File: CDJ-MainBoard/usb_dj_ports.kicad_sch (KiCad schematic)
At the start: 33 parts, among them J10 USB_DJ_STICK (USB3_A), J11 USB_SCREEN (USB3_A), J8 AUX POWER USB_A, J9 USB_C_Receptacle_USB2.0_16P, U1 Compute_Module_5_Functional, U3 AP2553W6-7, U4 AP2553W6-7, U5 AP2553W6-7, U6 USBLC6-2SC6, U7 USBLC6-2SC6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

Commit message: Add connectors for sections of inputs, and list of all inputs in XLSX
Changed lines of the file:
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@@
-	)
-	(junction
-		(at 35.56 167.64)
-		(diameter 0)
-		(color 0 0 0 0)
 	)
 	(junction
@@
 		)
 		(stroke
-			(width 0)
-			(type default)
-		)
-	)
-	(wire
-		(pts
-			(xy 35.56 167.64) (xy 30.48 167.64)
-		)
-		(stroke

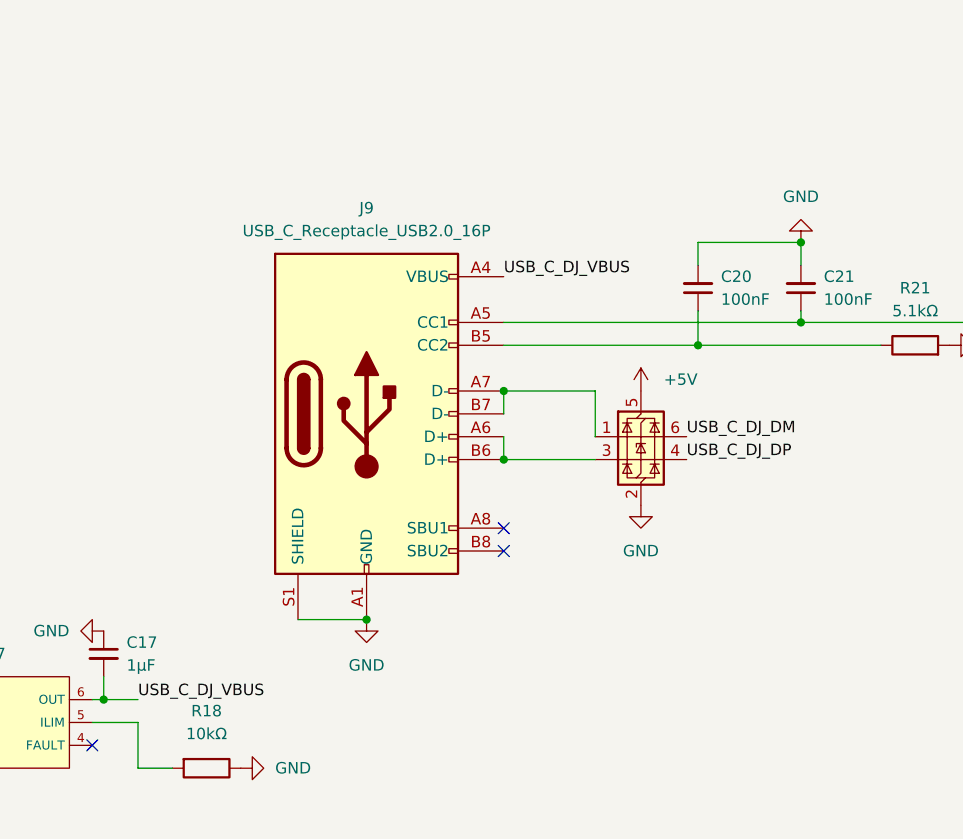
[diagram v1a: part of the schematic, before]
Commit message: Route the buck and fixed pinout on ethernet and 3D model offsets
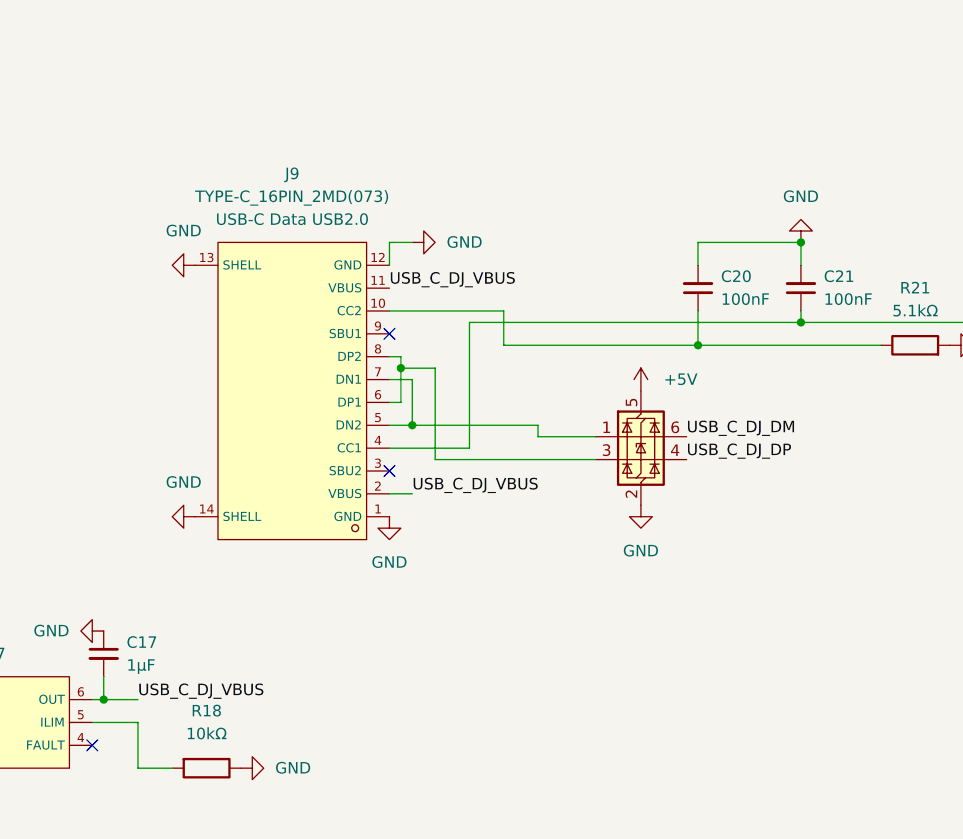
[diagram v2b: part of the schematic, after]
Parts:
- removed J9: USB_C_Receptacle_USB2.0_16P, JLC2KiCad_lib-footprints:USB-C-SMD_TYPE-C-6PIN-2MD-073, symbol Connector:USB_C_Receptacle_USB2.0_16P
- added J9: TYPE-C_16PIN_2MD(073), JLC2KiCad_lib-footprints:USB-C-SMD_TYPE-C-6PIN-2MD-073, symbol jlc_TYPE-C_16PIN_2MD(073):TYPE-C_16PIN_2MD(073)
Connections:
- net GND: now also J9.1 (GND), J9.12 (GND), J9.13 (SHELL), J9.14 (SHELL)
- net USB_C_DJ_VBUS: now also J9.11 (VBUS), J9.2 (VBUS)
- net at C21.1, R22.1: now also J9.4 (CC1)
- net at U6.3 (I/O2): now also J9.6 (DP1), J9.8 (DP2)
- net at U6.1 (I/O1): now also J9.5 (DN2), J9.7 (DN1)
- net at C20.1, R21.1: now also J9.10 (CC2)

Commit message: Route SD card and misc
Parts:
- removed U6, U7, U8: USBLC6-2SC6, PCM_JLCPCB:SOT-23-6_L2.9-W1.6-P0.95-LS2.8-BR, symbol Power_Protection:USBLC6-2SC6
- added U22, U6, U8: USBLC6-2SC6-ES, JLC2KiCad_lib-footprints:SOT-23-6_L2.9-W1.6-P0.95-LS2.8-BR, symbol jlc_USBLC6-2SC6-ES:USBLC6-2SC6-ES
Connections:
- net +5V: now also U22.5 (VCC), U6.5 (VCC), U8.5 (VCC)
- net GND: now also U22.2 (GND), U6.2 (GND), U8.2 (GND)
- net USB_C_DJ_DM: now also U22.3 (I/O2)
- net USB_C_DJ_DP: now also U22.1 (I/O1)
- net USB_DJ_DM: now also U8.6 (I/O1)
- net USB_DJ_DP: now also U8.4 (I/O2)
- net USB_SCR_DM: now also U6.6 (I/O1)
- net USB_SCR_DP: now also U6.4 (I/O2)
- net at J11.2 (D-): now also U6.1 (I/O1)
- net at J11.3 (D+): now also U6.3 (I/O2)
- net at J9.5 (DN2), J9.7 (DN1): now also U22.4 (I/O2)
- net at J9.6 (DP1), J9.8 (DP2): now also U22.6 (I/O1)
- net at J10.2 (D-): now also U8.1 (I/O1)
- net at J10.3 (D+): now also U8.3 (I/O2)
